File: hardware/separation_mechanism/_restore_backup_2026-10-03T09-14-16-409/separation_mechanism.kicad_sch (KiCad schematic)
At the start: 70 parts, among them IC1 74HC4052FT, J1 Conn_01x02_Socket, J3 USB_B, J4 Conn_01x02_Socket, J5 Micro_SD_Card_Det_Hirose_DM3AT, Q1 AO3400A, U1 L7805, U2 SAM-M10Q-00B, U3 SHT4x, U4 DPS368, U5 E22-900T30D_E220-900T22S(JP)_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, U6 FT4232H, U7 AP2112K-3.3, U8 93CxxB, Y1 12MHz

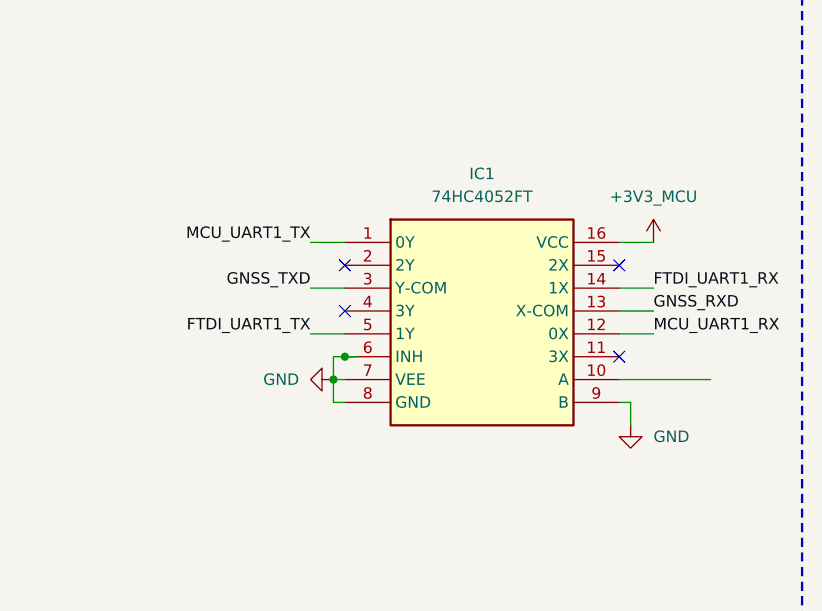
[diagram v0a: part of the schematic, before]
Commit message: feat(scm): 74HC4052 added.
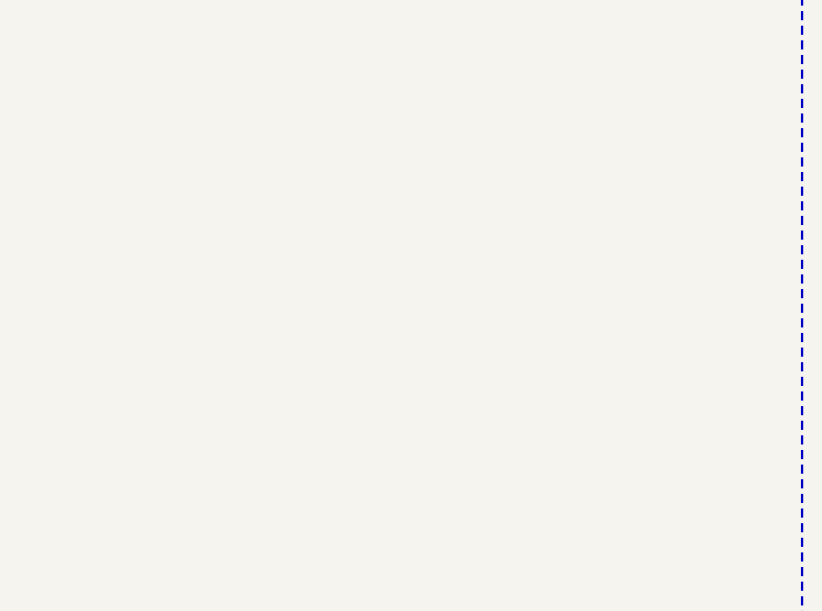
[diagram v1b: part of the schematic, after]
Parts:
- removed IC1: 74HC4052FT, SOP65P640X120-16N, symbol Unknown:74HC4052FT
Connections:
- no-connect marks 14 -> 10
